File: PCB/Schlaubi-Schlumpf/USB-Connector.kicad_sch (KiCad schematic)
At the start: 1 part, among them J7 TYPE-C-31-M-12

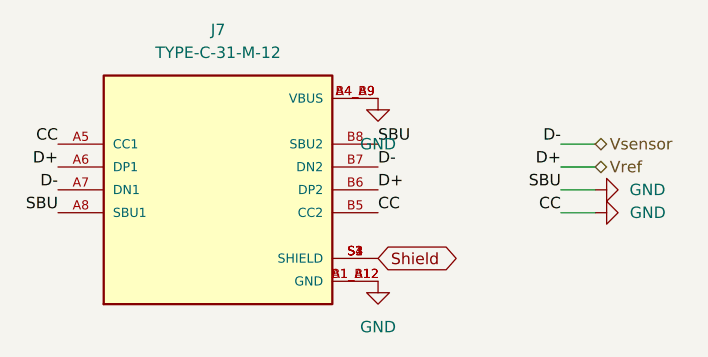
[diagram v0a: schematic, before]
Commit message: added IMU
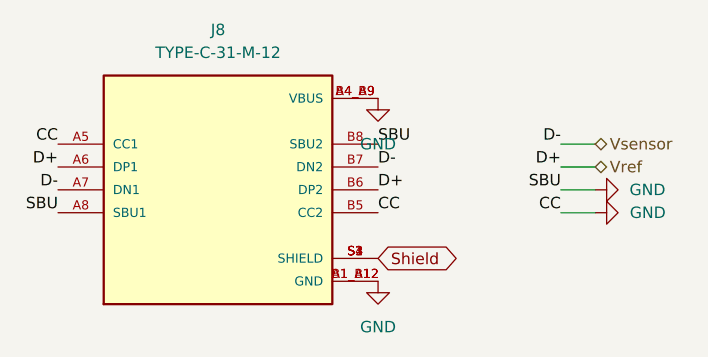
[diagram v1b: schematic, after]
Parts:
- renumbered J7 to J8
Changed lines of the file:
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@@
 		(dnp no)
 		(fields_autoplaced yes)
-		(property "Reference" "#PWR062"
+		(property "Reference" "#PWR066"
 			(at 187.96 86.36 0)
 			(effects
@@
 		(dnp no)
 		(fields_autoplaced yes)
-		(property "Reference" "#PWR055"
+		(property "Reference" "#PWR065"
 			(at 157.48 102.87 0)
 			(effects
@@
 		(dnp no)
 		(fields_autoplaced yes)
-		(property "Reference" "J7"
+		(property "Reference" "J8"
 			(at 139.7 68.58 0)
 			(effects
@@
 		(dnp no)
 		(fields_autoplaced yes)
-		(property "Reference" "#PWR063"
+		(property "Reference" "#PWR067"
 			(at 187.96 88.9 0)
 			(effects
@@
 		(dnp no)
 		(fields_autoplaced yes)
-		(property "Reference" "#PWR056"
+		(property "Reference" "#PWR064"
 			(at 157.48 82.55 0)
 			(effects
